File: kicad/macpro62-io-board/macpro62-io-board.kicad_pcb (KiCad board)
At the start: 6 copper layers, 101 x 173.6 mm, 142 parts, among them J1 IOB-HS1 MCIO 124 RA <- CB J3 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, J2 DISPLAY-LINK MCIO 74 RA <- Fa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, J25 ETH1 i226-V #1: ZJLQ-RJ45-SMD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, J26 ETH2 i226-V #2: ZJLQ-RJ45-SMD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, J28 Stock audio module connector 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, J29 Speaker 2P (stock lead; pitch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, J3 Stock PSU DC-out 12P (UNCONFI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, J30 Optional stock/remote power b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, J31 I/O-wall (821-2222) flex ZIF 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, J4 Stock PSU signal 6P (UNCONFIR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, J5 PSU pass-through -> BP J2 (12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, J6 IOB-LINK GH15 <- BP J6, J7 CONN_C fan + AirPort 2x20 @0.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, J8 Fan-assembly antenna coax: U.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, J9 Optional antenna pass-through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, SW1 DNP with the stock 821-2222-A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, SW2 DIAG button, T1 ETH1 2.5G magnetics JASN V24P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, T2 ETH2 2.5G magnetics JASN V24P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, U1 TPS65994AD PD #1 (C1, C2), U11 TUSB1046A C1 alt-mode mux/red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, U12 TUSB1046A C2 alt-mode mux/red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, U13 TUSB1046A C3 alt-mode mux/red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, U14 TUSB1046A C4 alt-mode mux/red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, U15 TUSB1046A C5 alt-mode mux/red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, U16 TUSB1046A C6 alt-mode mux/red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, U2 TPS65994AD PD #2 (C3, C4), U21 TUSB1002A A1 10G redriver, U22 TUSB1002A A2 10G redriver, U23 TUSB1002A A3 10G redriver, U24 TUSB1002A A4 10G redriver, U25 USB-A A1 VBUS switch 1.5 A (S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, U26 USB-A A2 VBUS switch 1.5 A (S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, U27 USB-A A3 VBUS switch 1.5 A (S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, U28 USB-A A4 VBUS switch 1.5 A (S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, U3 TPS65994AD PD #3 (C5, C6), U30 Hall A (DRV5032 class) - posi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, U31 Hall B (DRV5032 class) - posi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, U32 CH334R hub H1b (C4-C6 + codec), U33 CH334R hub H2 (A1-A4) <- IOB-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, U34 CH334R hub H1a (C1-C3 + H1b) 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, U35 CH334R hub H3 on H2 port 4: A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, U4 PD #1 config SPI flash (W25Q8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, U40 TPS259824ON eFuse 12 V in (15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, U41 TPS56C215 5V_C buck (USB-C VB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, U42 TPS56C215 5V_A buck (USB-A VB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, U43 TLV62585 3V3 (3 A) from 5V_SYS, U50 i226-V 2.5GbE (PCIe x1 from H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, U51 i226-V NVM SPI flash (size pe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, U52 i226-V #2 2.5GbE (PCIe x1 fro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, U53 i226-V #2 NVM SPI flash, U6 PD #2 config SPI flash, U60 TDP158 HDMI 2.0 retimer (GPU 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, U61 1V1 LDO (TDP158 core), U7 PD #3 config SPI flash, U70 C-Media CM108B USB audio code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, U71 PAM8302A mono class-D 2.5 W (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, U80 TLC59116 16-ch I2C LED driver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, U81 LIS2DH12 accelerometer (rotat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, U82 BL24C64A IOB ID EEPROM @0x51, U83 TCA9517 I2C buffer (I2C_SYS <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, U84 74LVC1G07 PD_INT -> IOB_INT_N, U90 EMC2101 fan controller @0x4C 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, U91 ASM1182e PCIe Gen2 switch: up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, Y1 12 MHz hub crystal, Y2 12 MHz hub crystal, Y3 12 MHz hub crystal, Y4 25 MHz (i226-V), Y5 12 MHz (CM108B), Y6 25 MHz (i226-V #2), Y7 12 MHz hub crystal (H3)

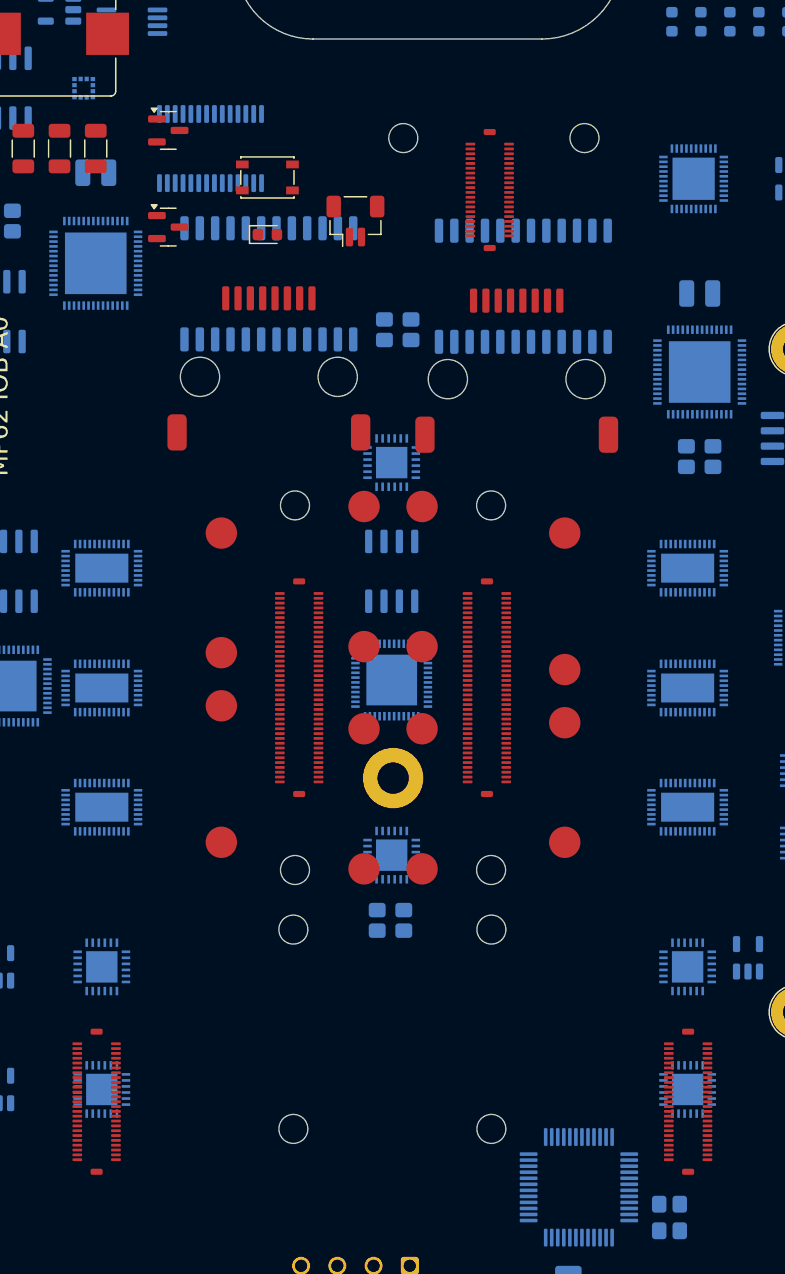
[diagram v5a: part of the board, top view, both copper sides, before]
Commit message: I/O: ports soldered on flex modules (no rigid PCB), DF40 50-pin standard port-module pinout with ID EEPROM, PA12 cradles + clamp plates, port axes square to plate (12.5 deg variant kept)
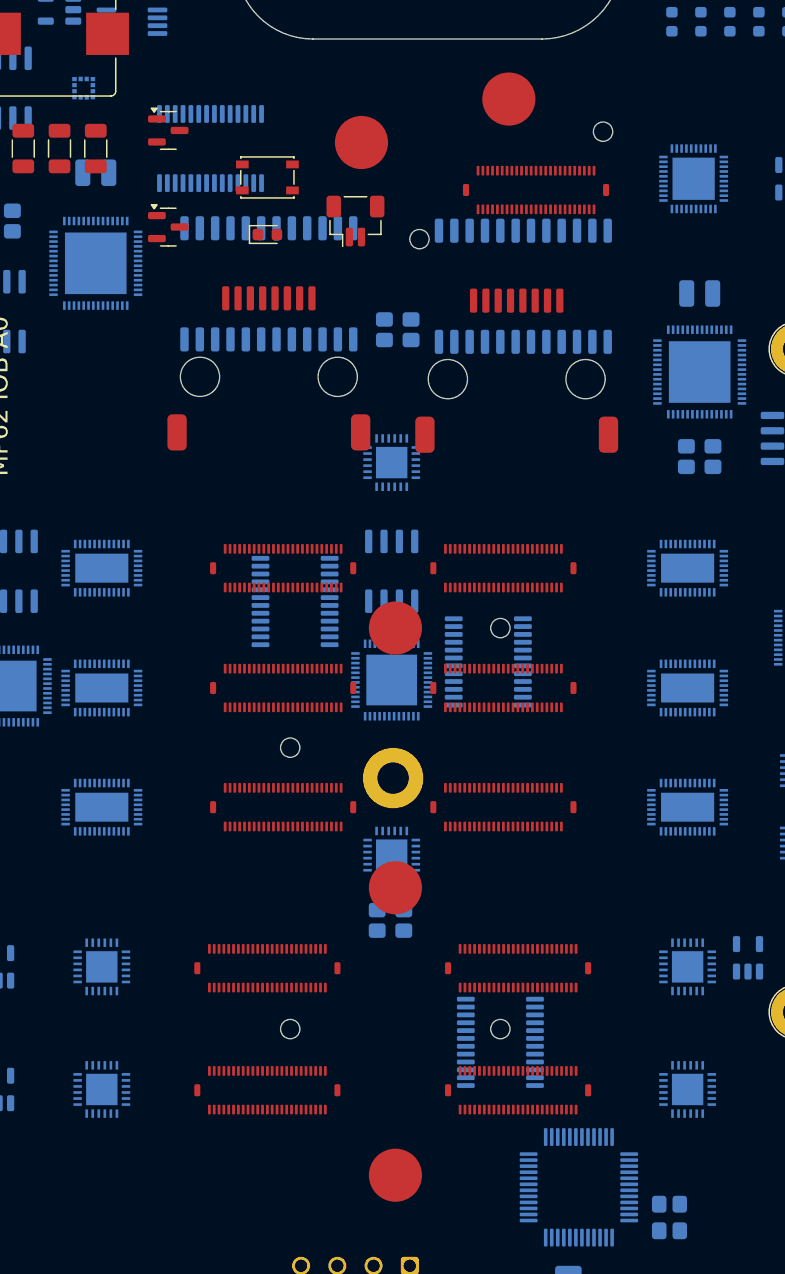
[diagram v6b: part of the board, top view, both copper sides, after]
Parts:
- removed H26: RA_H cradle M2 screw (printed PA12 wedge cradle), MP62_IO:MP62_Cradle_Screw_M2_NPTH
- removed H27, H28: RA_O cradle M2 screw (printed PA12 wedge cradle), MP62_IO:MP62_Cradle_Screw_M2_NPTH
- removed H29, H30: RH cradle M2 screw (printed PA12 wedge cradle), MP62_IO:MP62_Cradle_Screw_M2_NPTH
- removed JR1: RC_H riser link (C, ports C1/C2/C3, tilt -12.50 deg): DF40C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, MP62_IO:MP62_Hirose_DF40C-80DS-0.4V_PLACEHOLDER
- removed JR2: RC_O riser link (C, ports C4/C5/C6, tilt 12.50 deg): DF40C-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, MP62_IO:MP62_Hirose_DF40C-80DS-0.4V_PLACEHOLDER
- removed JR3: RA_H riser link (A, ports A1/A2, tilt -12.50 deg): DF40C-50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, MP62_IO:MP62_Hirose_DF40C-50DS-0.4V_PLACEHOLDER
- removed JR4: RA_O riser link (A, ports A3/A4, tilt 12.50 deg): DF40C-50D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, MP62_IO:MP62_Hirose_DF40C-50DS-0.4V_PLACEHOLDER
- removed JR5: RH riser link (HDMI, ports HDMI, tilt -12.50 deg): DF40C-40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, MP62_IO:MP62_Hirose_DF40C-40DS-0.4V_PLACEHOLDER
- removed PG1: RC_H pogo VBUS_C3, working height 4.79, length class P-S, MP62_IO:MP62_Pogo_SMD_D2.0_PLACEHOLDER
- removed PG10: RC_O pogo VBUS_C3, working height 7.38, length class P-L, MP62_IO:MP62_Pogo_SMD_D2.0_PLACEHOLDER
- removed PG11: RC_O pogo VBUS_C2, working height 4.77, length class P-S, MP62_IO:MP62_Pogo_SMD_D2.0_PLACEHOLDER
- removed PG12: RC_O pogo VBUS_C2, working height 7.38, length class P-L, MP62_IO:MP62_Pogo_SMD_D2.0_PLACEHOLDER
- removed PG13: RC_O pogo VBUS_C1, working height 4.77, length class P-S, MP62_IO:MP62_Pogo_SMD_D2.0_PLACEHOLDER
- removed PG14: RC_O pogo VBUS_C1, working height 7.38, length class P-L, MP62_IO:MP62_Pogo_SMD_D2.0_PLACEHOLDER
- removed PG15: RC_O pogo GND, working height 4.77, length class P-S, MP62_IO:MP62_Pogo_SMD_D2.0_PLACEHOLDER
- removed PG16: RC_O pogo GND, working height 7.38, length class P-L, MP62_IO:MP62_Pogo_SMD_D2.0_PLACEHOLDER
- removed PG2: RC_H pogo VBUS_C3, working height 7.41, length class P-L, MP62_IO:MP62_Pogo_SMD_D2.0_PLACEHOLDER
- removed PG3: RC_H pogo VBUS_C2, working height 4.79, length class P-S, MP62_IO:MP62_Pogo_SMD_D2.0_PLACEHOLDER
- removed PG4: RC_H pogo VBUS_C2, working height 7.41, length class P-L, MP62_IO:MP62_Pogo_SMD_D2.0_PLACEHOLDER
- removed PG5: RC_H pogo VBUS_C1, working height 4.79, length class P-S, MP62_IO:MP62_Pogo_SMD_D2.0_PLACEHOLDER
- removed PG6: RC_H pogo VBUS_C1, working height 7.41, length class P-L, MP62_IO:MP62_Pogo_SMD_D2.0_PLACEHOLDER
- removed PG7: RC_H pogo GND, working height 4.79, length class P-S, MP62_IO:MP62_Pogo_SMD_D2.0_PLACEHOLDER
- removed PG8: RC_H pogo GND, working height 7.41, length class P-L, MP62_IO:MP62_Pogo_SMD_D2.0_PLACEHOLDER
- removed PG9: RC_O pogo VBUS_C3, working height 4.77, length class P-S, MP62_IO:MP62_Pogo_SMD_D2.0_PLACEHOLDER
- added H40: port-module cradle locating peg D1.5, MP62_IO:MP62_Cradle_Peg_D1.6_NPTH, F.Cu at (96.5, 129.2)
- added H41: port-module cradle locating peg D1.5, MP62_IO:MP62_Cradle_Peg_D1.6_NPTH, F.Cu at (79.1, 139.1)
- added H42: port-module cradle locating peg D1.5, MP62_IO:MP62_Cradle_Peg_D1.6_NPTH, F.Cu at (96.5, 162.4)
- added H43: port-module cradle locating peg D1.5, MP62_IO:MP62_Cradle_Peg_D1.6_NPTH, F.Cu at (79.1, 162.4)
- added H44: port-module cradle locating peg D1.5, MP62_IO:MP62_Cradle_Peg_D1.6_NPTH, F.Cu at (105.0, 88.1)
- added H45: port-module cradle locating peg D1.5, MP62_IO:MP62_Cradle_Peg_D1.6_NPTH, F.Cu at (89.8, 97.0)
- added JM1: MOD-C slot C1: DF40C-50DS-0.4V(51) C424646 (PMI-50) <- modu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, MP62_IO:MP62_Hirose_DF40C-50DS-0.4V_PLACEHOLDER, F.Cu at (96.8, 124.2)
- added JM10: MOD-A slot A4: DF40C-50DS-0.4V(51) C424646 (PMI-50) <- modu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, MP62_IO:MP62_Hirose_DF40C-50DS-0.4V_PLACEHOLDER, F.Cu at (77.2, 167.5)
- added JM11: MOD-H slot HDMI: DF40C-50DS-0.4V(51) C424646 (PMI-50) <- mo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, MP62_IO:MP62_Hirose_DF40C-50DS-0.4V_PLACEHOLDER, F.Cu at (99.5, 92.9)
- added JM2: MOD-C slot C2: DF40C-50DS-0.4V(51) C424646 (PMI-50) <- modu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, MP62_IO:MP62_Hirose_DF40C-50DS-0.4V_PLACEHOLDER, F.Cu at (96.8, 134.2)
- added JM3: MOD-C slot C3: DF40C-50DS-0.4V(51) C424646 (PMI-50) <- modu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, MP62_IO:MP62_Hirose_DF40C-50DS-0.4V_PLACEHOLDER, F.Cu at (96.8, 144.0)
- added JM4: MOD-C slot C4: DF40C-50DS-0.4V(51) C424646 (PMI-50) <- modu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, MP62_IO:MP62_Hirose_DF40C-50DS-0.4V_PLACEHOLDER, F.Cu at (78.5, 124.2)
- added JM5: MOD-C slot C5: DF40C-50DS-0.4V(51) C424646 (PMI-50) <- modu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, MP62_IO:MP62_Hirose_DF40C-50DS-0.4V_PLACEHOLDER, F.Cu at (78.5, 134.2)
- added JM6: MOD-C slot C6: DF40C-50DS-0.4V(51) C424646 (PMI-50) <- modu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, MP62_IO:MP62_Hirose_DF40C-50DS-0.4V_PLACEHOLDER, F.Cu at (78.5, 144.0)
- added JM7: MOD-A slot A1: DF40C-50DS-0.4V(51) C424646 (PMI-50) <- modu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, MP62_IO:MP62_Hirose_DF40C-50DS-0.4V_PLACEHOLDER, F.Cu at (98.0, 157.4)
- added JM8: MOD-A slot A2: DF40C-50DS-0.4V(51) C424646 (PMI-50) <- modu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, MP62_IO:MP62_Hirose_DF40C-50DS-0.4V_PLACEHOLDER, F.Cu at (98.0, 167.5)
- added JM9: MOD-A slot A3: DF40C-50DS-0.4V(51) C424646 (PMI-50) <- modu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, MP62_IO:MP62_Hirose_DF40C-50DS-0.4V_PLACEHOLDER, F.Cu at (77.2, 157.4)
- added U95: TCA9548A @0x70: module ID I2C ch0-5 = C1-C6, ch6-7 = A1-A2, MP62_IO:TSSOP-24_4.4x7.8mm_P0.65mm, B.Cu at (95.5, 132.0)
- added U96: TCA9548A @0x71: module ID I2C ch0-1 = A3-A4, ch2 = HDMI, ch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, MP62_IO:TSSOP-24_4.4x7.8mm_P0.65mm, B.Cu at (96.5, 163.5)
- added U97: TCA9555 @0x27 on U96 ch3 (private): PRSNT# of the 11 port m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, MP62_IO:TSSOP-24_4.4x7.8mm_P0.65mm, B.Cu at (79.5, 127.0)
- H21: value RC_H cradle M2 screw (printed PA12 wedge cradle) -> port-module clamp post (C): M2 SMT nut, clamp screw through plate + cradle post; footprint MP62_IO:MP62_Cradle_Screw_M2_NPTH -> MP62_IO:MP62_Cradle_Nut_M2_SMT_PLACEHOLDER
- H22: value RC_H cradle M2 screw (printed PA12 wedge cradle) -> port-module clamp post (C+A): M2 SMT nut, clamp screw through plate + cradle post; footprint MP62_IO:MP62_Cradle_Screw_M2_NPTH -> MP62_IO:MP62_Cradle_Nut_M2_SMT_PLACEHOLDER
- H23: value RC_O cradle M2 screw (printed PA12 wedge cradle) -> port-module clamp post (A): M2 SMT nut, clamp screw through plate + cradle post; footprint MP62_IO:MP62_Cradle_Screw_M2_NPTH -> MP62_IO:MP62_Cradle_Nut_M2_SMT_PLACEHOLDER
- H24: value RC_O cradle M2 screw (printed PA12 wedge cradle) -> port-module clamp post (HDMI): M2 SMT nut, clamp screw through plate + cradle post; footprint MP62_IO:MP62_Cradle_Screw_M2_NPTH -> MP62_IO:MP62_Cradle_Nut_M2_SMT_PLACEHOLDER
- H25: value RA_H cradle M2 screw (printed PA12 wedge cradle) -> port-module clamp post (HDMI): M2 SMT nut, clamp screw through plate + cradle post; footprint MP62_IO:MP62_Cradle_Screw_M2_NPTH -> MP62_IO:MP62_Cradle_Nut_M2_SMT_PLACEHOLDER
- moved H25 82.4 mm to (85.0, 89.0)
- moved H24 38.0 mm to (97.2, 85.4)
- moved H22 32.6 mm to (87.8, 150.7)
- moved H23 26.6 mm to (87.8, 174.5)
- moved H21 21.5 mm to (87.8, 129.2)
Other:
- board text added: "A1 MOD-A"
- board text added: "A2 MOD-A"
- board text added: "A3 MOD-A"
- board text added: "A4 MOD-A"
- board text added: "C1 MOD-C"
- board text added: "C2 MOD-C"
- board text added: "C3 MOD-C"
- board text added: "C4 MOD-C"
- board text added: "C5 MOD-C"
- board text added: "C6 MOD-C"
- board text added: "D0 = 18.0 crown / 16.5 edge: USB-C/USB-A/HDMI = swappable FPC port modules (D-IO16) on printed cradles, axis normal to the plate, JMn DF40C-50DS per module; RJ45 face <= 13.6."
- board text added: "HDMI MOD-H"
- board text added: "RJ45 vertical on the main board; USB-C/USB-A/HDMI on FPC modules (plan 4.7.9). Dwgs.User: module stiffener outlines + C-fold envelopes."
- board text removed: "All ports are VERTICAL (mating axis normal to the board); the plate is curved with no lands (stock flex must lie flat), mouths flush at the outboard edge (plan 4.4/4.7)."
- board text removed: "D0 = 18.0 crown / 16.5 edge: USB-C/USB-A/HDMI need 17.2-17.9 board-to-mouth -> port risers (+2.2..2.9) under 15.0 parts; RJ45 face <= 13.6 (plan 4.7.4)."
- board text removed: "RA_H riser -12.5 deg"
- board text removed: "RA_O riser 12.5 deg"
- board text removed: "RC_H riser -12.5 deg"
- board text removed: "RC_O riser 12.5 deg"
- board text removed: "RH riser -12.5 deg"

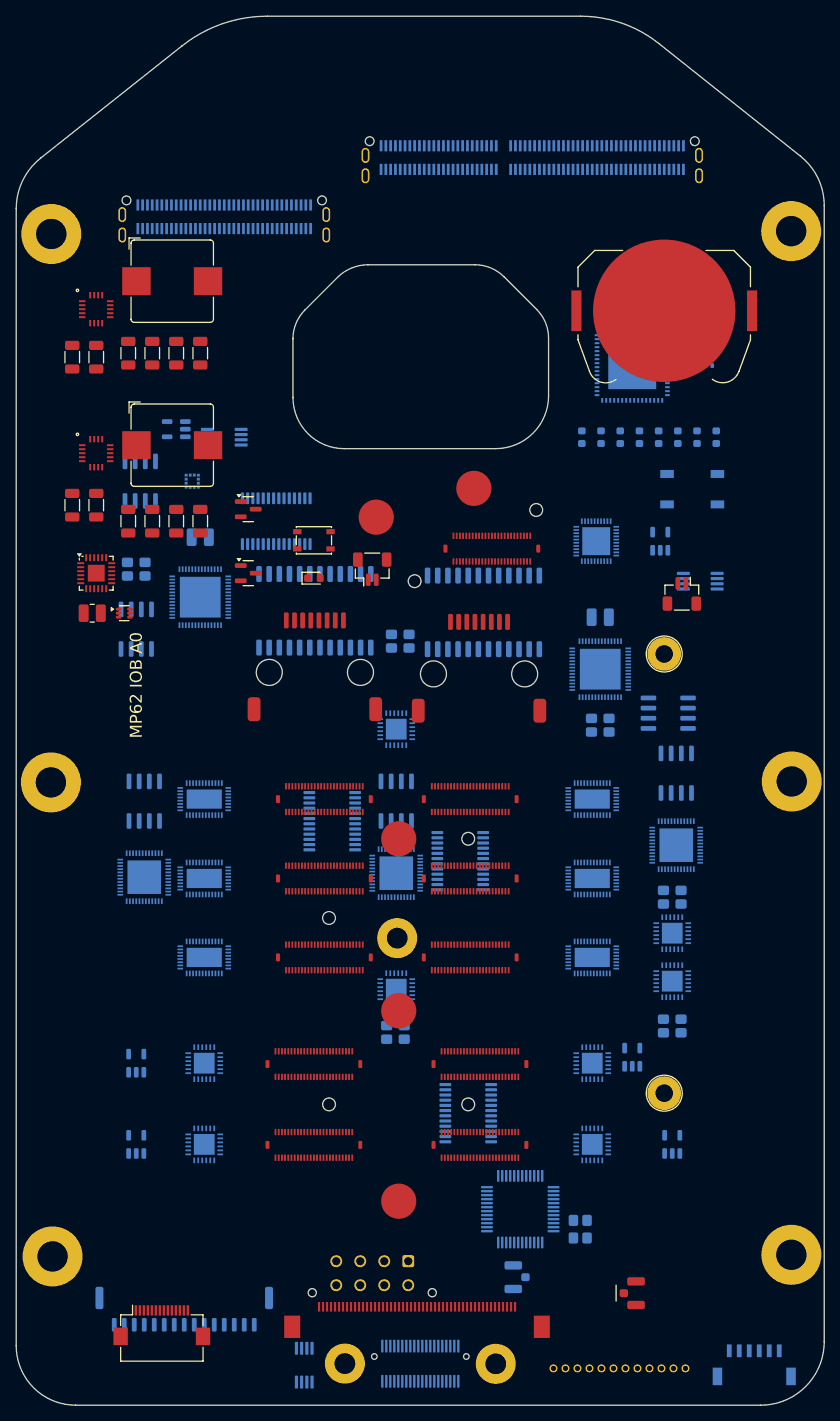
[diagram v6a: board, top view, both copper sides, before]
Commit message: I/O plate: centre + corner M1.6 frame screws, screwpt variant, plate fixes, module routing, ESD
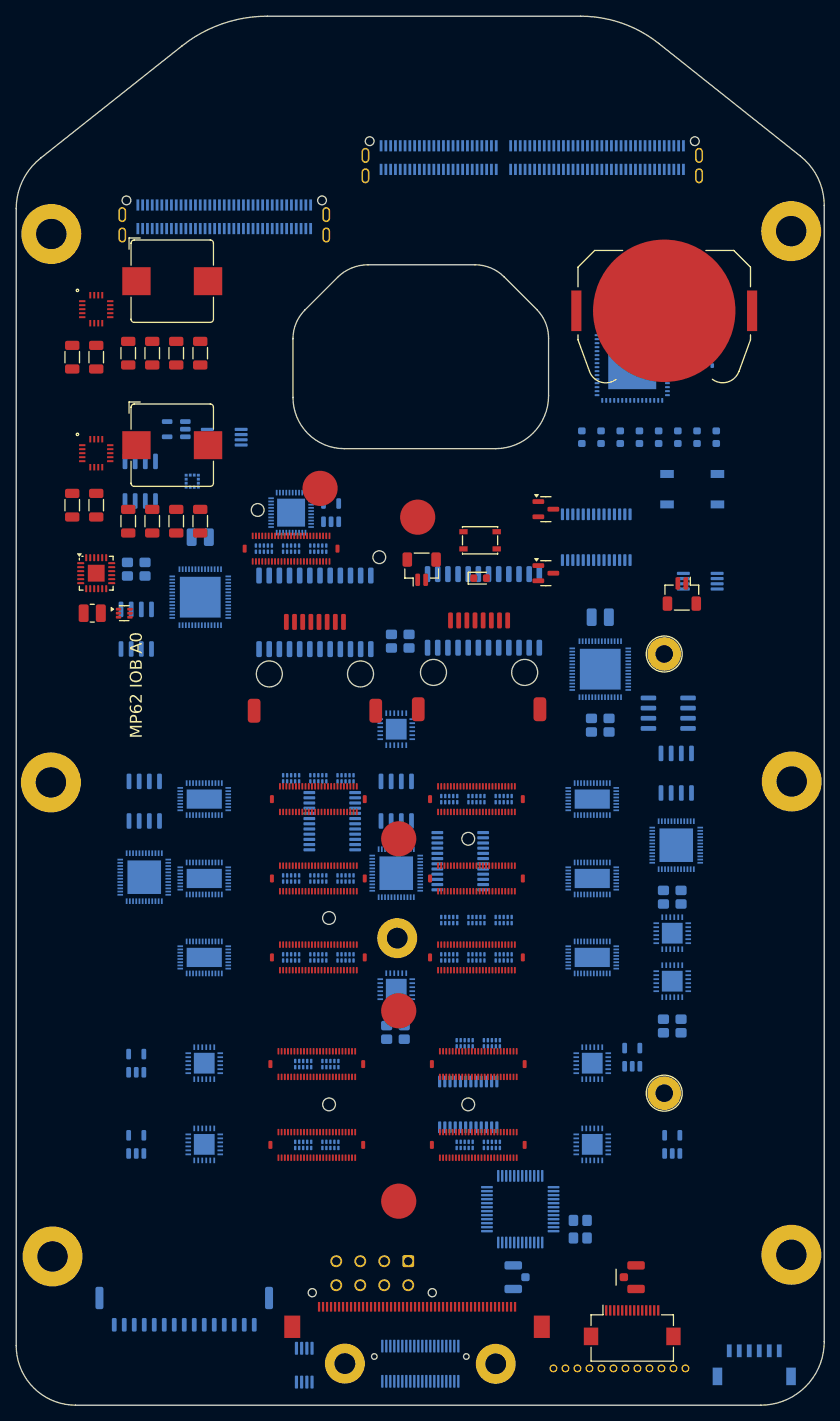
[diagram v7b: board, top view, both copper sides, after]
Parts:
- added D200: ESD C1 (TPD4E02B04DQAR C106794), MP62_IO:USON-10_2.5x1.0mm_P0.5mm, B.Cu at (100.9, 124.2)
- added D201: ESD C1 (TPD4E02B04DQAR C106794), MP62_IO:USON-10_2.5x1.0mm_P0.5mm, B.Cu at (97.5, 124.2)
- added D202: ESD C1 (TPD4E05U06DQAR C138714), MP62_IO:USON-10_2.5x1.0mm_P0.5mm, B.Cu at (94.1, 124.2)
- added D203: ESD C2 (TPD4E02B04DQAR C106794), MP62_IO:USON-10_2.5x1.0mm_P0.5mm, B.Cu at (100.9, 139.4)
- added D204: ESD C2 (TPD4E02B04DQAR C106794), MP62_IO:USON-10_2.5x1.0mm_P0.5mm, B.Cu at (97.5, 139.4)
- added D205: ESD C2 (TPD4E05U06DQAR C138714), MP62_IO:USON-10_2.5x1.0mm_P0.5mm, B.Cu at (94.1, 139.4)
- added D206: ESD C3 (TPD4E02B04DQAR C106794), MP62_IO:USON-10_2.5x1.0mm_P0.5mm, B.Cu at (100.9, 144.0)
- added D207: ESD C3 (TPD4E02B04DQAR C106794), MP62_IO:USON-10_2.5x1.0mm_P0.5mm, B.Cu at (97.5, 144.0)
- added D208: ESD C3 (TPD4E05U06DQAR C138714), MP62_IO:USON-10_2.5x1.0mm_P0.5mm, B.Cu at (94.1, 144.0)
- added D209: ESD C4 (TPD4E02B04DQAR C106794), MP62_IO:USON-10_2.5x1.0mm_P0.5mm, B.Cu at (81.2, 121.6)
- added D210: ESD C4 (TPD4E02B04DQAR C106794), MP62_IO:USON-10_2.5x1.0mm_P0.5mm, B.Cu at (77.8, 121.6)
- added D211: ESD C4 (TPD4E05U06DQAR C138714), MP62_IO:USON-10_2.5x1.0mm_P0.5mm, B.Cu at (74.4, 121.6)
- added D212: ESD C5 (TPD4E02B04DQAR C106794), MP62_IO:USON-10_2.5x1.0mm_P0.5mm, B.Cu at (81.2, 134.2)
- added D213: ESD C5 (TPD4E02B04DQAR C106794), MP62_IO:USON-10_2.5x1.0mm_P0.5mm, B.Cu at (77.8, 134.2)
- added D214: ESD C5 (TPD4E05U06DQAR C138714), MP62_IO:USON-10_2.5x1.0mm_P0.5mm, B.Cu at (74.4, 134.2)
- added D215: ESD C6 (TPD4E02B04DQAR C106794), MP62_IO:USON-10_2.5x1.0mm_P0.5mm, B.Cu at (81.2, 144.0)
- added D216: ESD C6 (TPD4E02B04DQAR C106794), MP62_IO:USON-10_2.5x1.0mm_P0.5mm, B.Cu at (77.8, 144.0)
- added D217: ESD C6 (TPD4E05U06DQAR C138714), MP62_IO:USON-10_2.5x1.0mm_P0.5mm, B.Cu at (74.4, 144.0)
- added D218: ESD A1 (TPD4E02B04DQAR C106794), MP62_IO:USON-10_2.5x1.0mm_P0.5mm, B.Cu at (99.5, 154.8)
- added D219: ESD A1 (TPD4E05U06DQAR C138714), MP62_IO:USON-10_2.5x1.0mm_P0.5mm, B.Cu at (96.1, 154.8)
- added D220: ESD A2 (TPD4E02B04DQAR C106794), MP62_IO:USON-10_2.5x1.0mm_P0.5mm, B.Cu at (99.5, 167.5)
- added D221: ESD A2 (TPD4E05U06DQAR C138714), MP62_IO:USON-10_2.5x1.0mm_P0.5mm, B.Cu at (96.1, 167.5)
- added D222: ESD A3 (TPD4E02B04DQAR C106794), MP62_IO:USON-10_2.5x1.0mm_P0.5mm, B.Cu at (79.3, 157.4)
- added D223: ESD A3 (TPD4E05U06DQAR C138714), MP62_IO:USON-10_2.5x1.0mm_P0.5mm, B.Cu at (75.9, 157.4)
- added D224: ESD A4 (TPD4E02B04DQAR C106794), MP62_IO:USON-10_2.5x1.0mm_P0.5mm, B.Cu at (79.3, 167.5)
- added D225: ESD A4 (TPD4E05U06DQAR C138714), MP62_IO:USON-10_2.5x1.0mm_P0.5mm, B.Cu at (75.9, 167.5)
- added D226: ESD HDMI (TPD4E05U06DQAR C138714), MP62_IO:USON-10_2.5x1.0mm_P0.5mm, B.Cu at (77.8, 92.9)
- added D227: ESD HDMI (TPD4E05U06DQAR C138714), MP62_IO:USON-10_2.5x1.0mm_P0.5mm, B.Cu at (74.4, 92.9)
- added D228: ESD HDMI (TPD4E05U06DQAR C138714), MP62_IO:USON-10_2.5x1.0mm_P0.5mm, B.Cu at (71.0, 92.9)
- JM1: value MOD-C slot C1: DF40C-50DS-0.4V(51) C424646 (PMI-50) <- module DF40C-50DP C424645 on the C-folded tail (module as drawn,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 -> MOD-C slot C1: DF40C-50DS-0.4V(51) C424646 (PMI-50 v2) <- module DF40C-50DP C424645 on the folded tail (JM rot 180, axi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
- JM10: value MOD-A slot A4: DF40C-50DS-0.4V(51) C424646 (PMI-50) <- module DF40C-50DP C424645 on the C-folded tail (module rot 180, 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 -> MOD-A slot A4: DF40C-50DS-0.4V(51) C424646 (PMI-50 v2) <- module DF40C-50DP C424645 on the folded tail (JM rot 0, axis 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
- JM11: value MOD-H slot HDMI: DF40C-50DS-0.4V(51) C424646 (PMI-50) <- module DF40C-50DP C424645 on the C-folded tail (module as draw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 -> MOD-H slot HDMI: DF40C-50DS-0.4V(51) C424646 (PMI-50 v2) <- module DF40C-50DP C424645 on the folded tail (JM rot 0, axi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
- JM2: value MOD-C slot C2: DF40C-50DS-0.4V(51) C424646 (PMI-50) <- module DF40C-50DP C424645 on the C-folded tail (module as drawn,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 -> MOD-C slot C2: DF40C-50DS-0.4V(51) C424646 (PMI-50 v2) <- module DF40C-50DP C424645 on the folded tail (JM rot 180, axi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
- JM3: value MOD-C slot C3: DF40C-50DS-0.4V(51) C424646 (PMI-50) <- module DF40C-50DP C424645 on the C-folded tail (module as drawn,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 -> MOD-C slot C3: DF40C-50DS-0.4V(51) C424646 (PMI-50 v2) <- module DF40C-50DP C424645 on the folded tail (JM rot 180, axi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
- JM4: value MOD-C slot C4: DF40C-50DS-0.4V(51) C424646 (PMI-50) <- module DF40C-50DP C424645 on the C-folded tail (module rot 180, 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 -> MOD-C slot C4: DF40C-50DS-0.4V(51) C424646 (PMI-50 v2) <- module DF40C-50DP C424645 on the folded tail (JM rot 0, axis 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
- JM5: value MOD-C slot C5: DF40C-50DS-0.4V(51) C424646 (PMI-50) <- module DF40C-50DP C424645 on the C-folded tail (module rot 180, 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 -> MOD-C slot C5: DF40C-50DS-0.4V(51) C424646 (PMI-50 v2) <- module DF40C-50DP C424645 on the folded tail (JM rot 0, axis 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
- JM6: value MOD-C slot C6: DF40C-50DS-0.4V(51) C424646 (PMI-50) <- module DF40C-50DP C424645 on the C-folded tail (module rot 180, 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 -> MOD-C slot C6: DF40C-50DS-0.4V(51) C424646 (PMI-50 v2) <- module DF40C-50DP C424645 on the folded tail (JM rot 0, axis 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
- JM7: value MOD-A slot A1: DF40C-50DS-0.4V(51) C424646 (PMI-50) <- module DF40C-50DP C424645 on the C-folded tail (module as drawn,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 -> MOD-A slot A1: DF40C-50DS-0.4V(51) C424646 (PMI-50 v2) <- module DF40C-50DP C424645 on the folded tail (JM rot 180, axi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
- JM8: value MOD-A slot A2: DF40C-50DS-0.4V(51) C424646 (PMI-50) <- module DF40C-50DP C424645 on the C-folded tail (module as drawn,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 -> MOD-A slot A2: DF40C-50DS-0.4V(51) C424646 (PMI-50 v2) <- module DF40C-50DP C424645 on the folded tail (JM rot 180, axi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
- JM9: value MOD-A slot A3: DF40C-50DS-0.4V(51) C424646 (PMI-50) <- module DF40C-50DP C424645 on the C-folded tail (module rot 180, 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 -> MOD-A slot A3: DF40C-50DS-0.4V(51) C424646 (PMI-50 v2) <- module DF40C-50DP C424645 on the folded tail (JM rot 0, axis 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
- U60: value TDP158 HDMI 2.0 retimer (GPU link 2) -> TDP158 HDMI 2.0 retimer (GPU link 2), next to the HDMI JM
- moved J31 58.8 mm to (117.0, 190.0)
- moved U61 41.3 mm to (79.4, 88.4)
- moved U80 40.0 mm to (112.5, 91.5)
- moved U60 38.3 mm to (74.4, 88.4)
- moved U30 37.2 mm to (106.2, 88.0)
- moved U31 37.2 mm to (106.2, 96.0)
- moved H44 34.8 mm to (70.2, 88.1)
- moved JM11 25.1 mm to (74.4, 92.9)
- moved D20 20.8 mm to (98.0, 96.6)
- moved SW1 20.8 mm to (98.0, 91.9)
- moved H24 19.2 mm to (78.0, 85.4)
- moved J30 6.18 mm to (90.7, 95.5)
- moved H45 5.34 mm to (85.4, 94.0)
- moved H25 5.18 mm to (90.2, 89.0)
- moved J9 2.00 mm to (117.0, 184.0)
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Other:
- board text added: "A1 loop fold: no F parts (> 0.57)"
- board text added: "A2 loop fold: no F parts (> 0.57)"
- board text added: "A3 loop fold: no F parts (> 0.53)"
- board text added: "A4 loop fold: no F parts (> 0.53)"
- board text added: "Port grid (stock flex cut-outs, scan 2026-10-02, MIRRORED to the true back view 2026-10-02 per the outer-face scan): USB-C X 43.13 / 63.73, Y 75.76 / 65.84 / 55.97; USB-A 43.06 / 63.70, Y 42.64 / 32.54; RJ45 ETH2 (43.15,91.60) / ETH1 (63.66,91.41); HDMI (63.86,107.07); button (43.02,108.11)."
- board text removed: "Port grid (stock flex cut-outs, scan 2026-10-02): USB-C Xb 43.09 / 63.69, Y 75.76 / 65.84 / 55.97; USB-A 43.12 / 63.76, Y 42.64 / 32.54; RJ45 (43.15,91.41)/(63.67,91.60); HDMI (42.96,107.07); button (63.79,108.11)."
